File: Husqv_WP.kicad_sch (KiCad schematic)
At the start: 10 parts, among them U1 TC4421, U2 TC4422

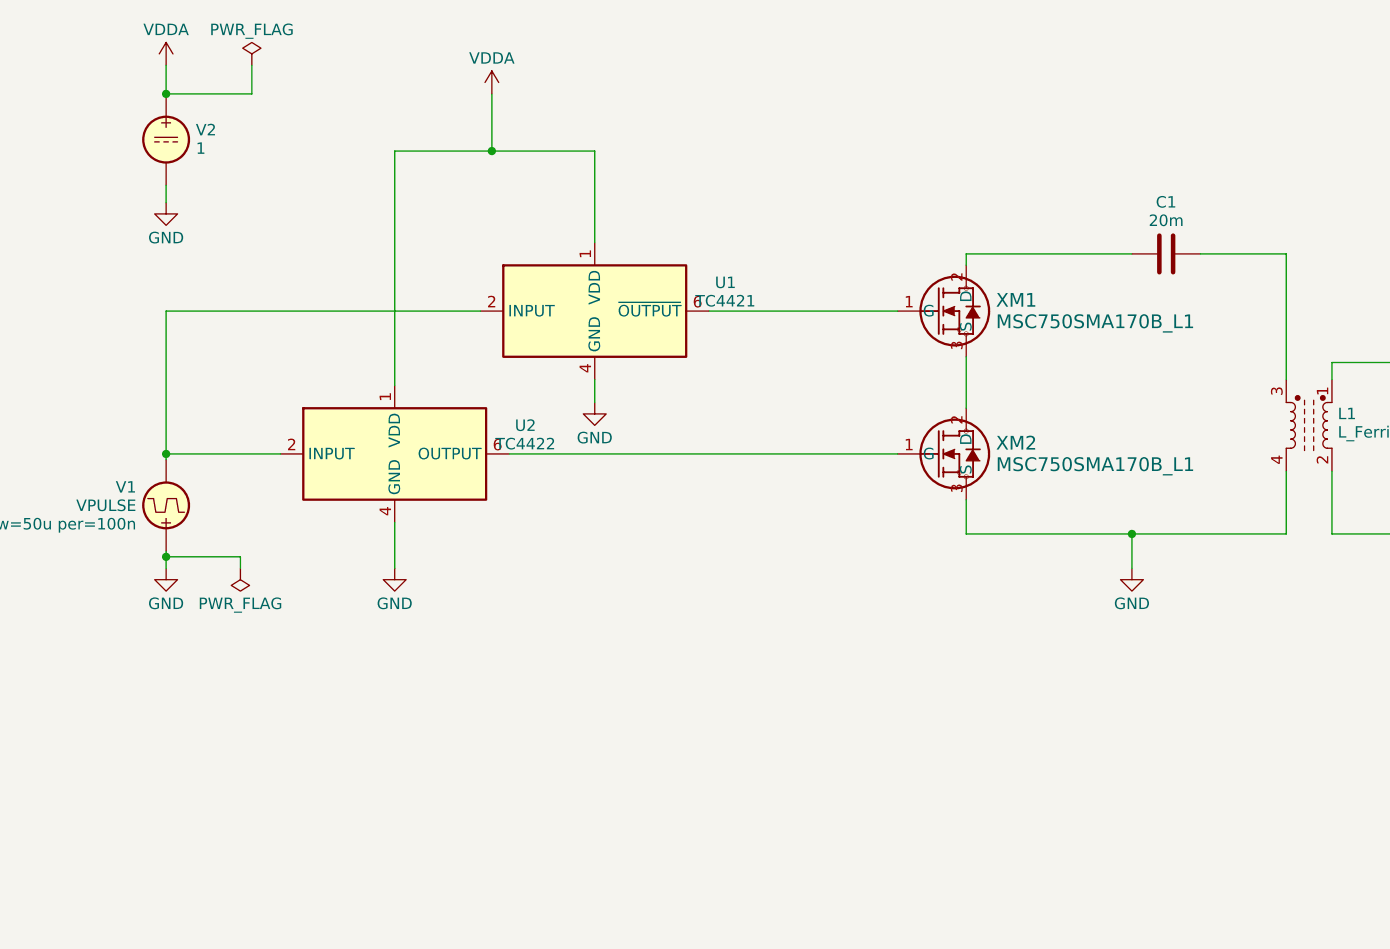
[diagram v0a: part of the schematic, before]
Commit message: working ... and changing branch names for new LLC topologies (so I can use only low-side FET drivers)
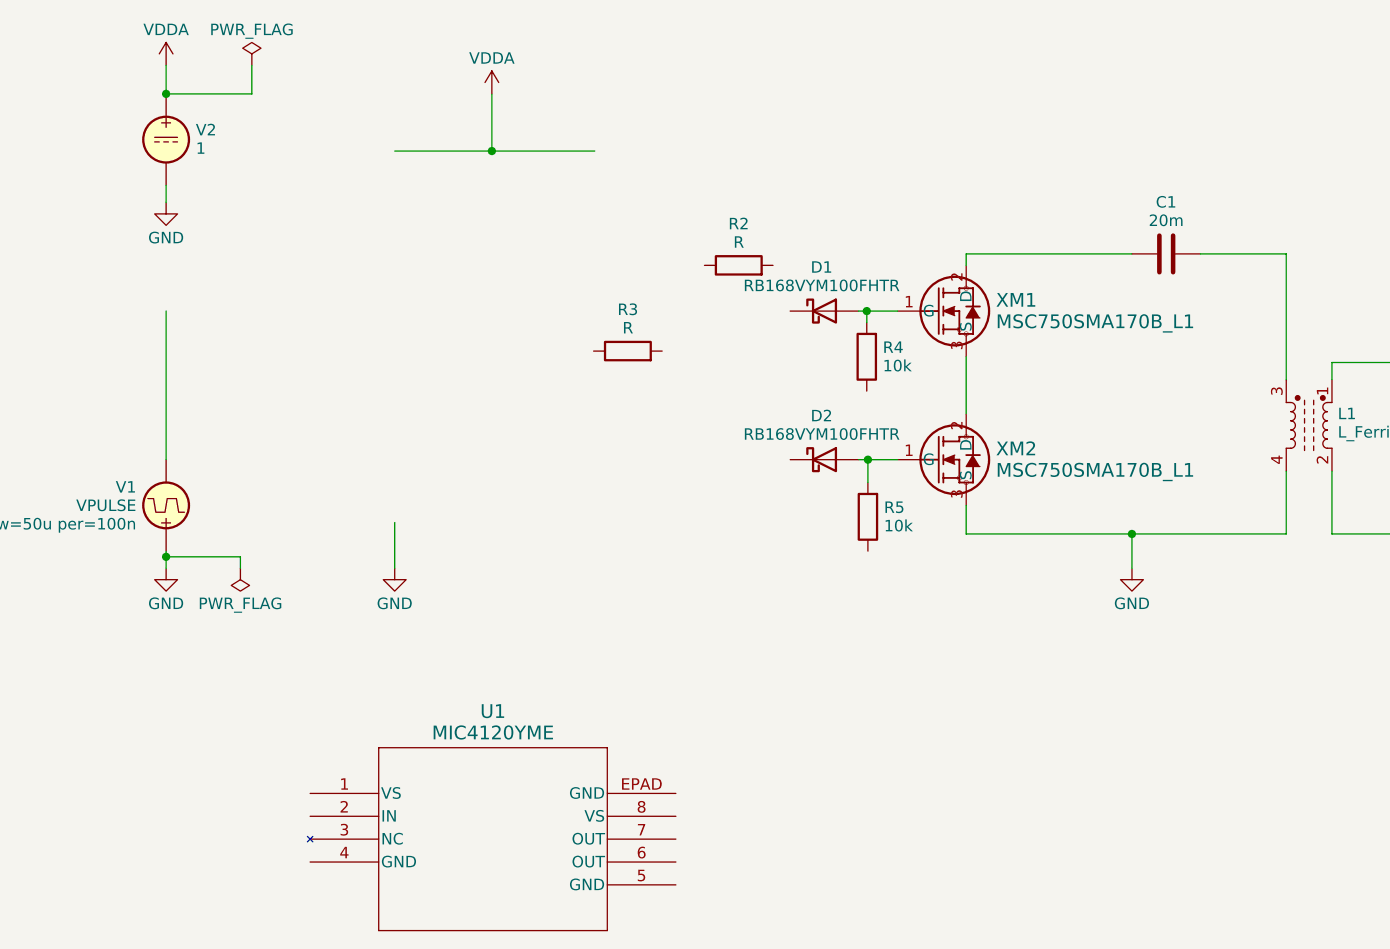
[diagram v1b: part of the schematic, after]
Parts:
- removed U1: TC4421, Package_DIP:DIP-8-N6_W7.62mm, symbol Driver_FET:TC4421
- removed U2: TC4422, Package_DIP:DIP-8-N6_W7.62mm, symbol Driver_FET:TC4422
- added D1, D2: RB168VYM100FHTR, Diode_SMD:D_SOD-323_HandSoldering, symbol Device:D_Schottky
- added R2, R3: R, symbol Device:R
- added R4, R5: 10k, Resistor_SMD:R_0603_1608Metric_Pad0.98x0.95mm_HandSolder, symbol Device:R
- added U1: MIC4120YME, SOIC8_EPAD_ME_MCH, symbol myLibSymbols:MIC4120YME
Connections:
- net at XM1.1 (G): now also D1.2 (A), R4.2
- net at XM2.1 (G): now also D2.2 (A), R5.2
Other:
- moved on the sheet: XM2

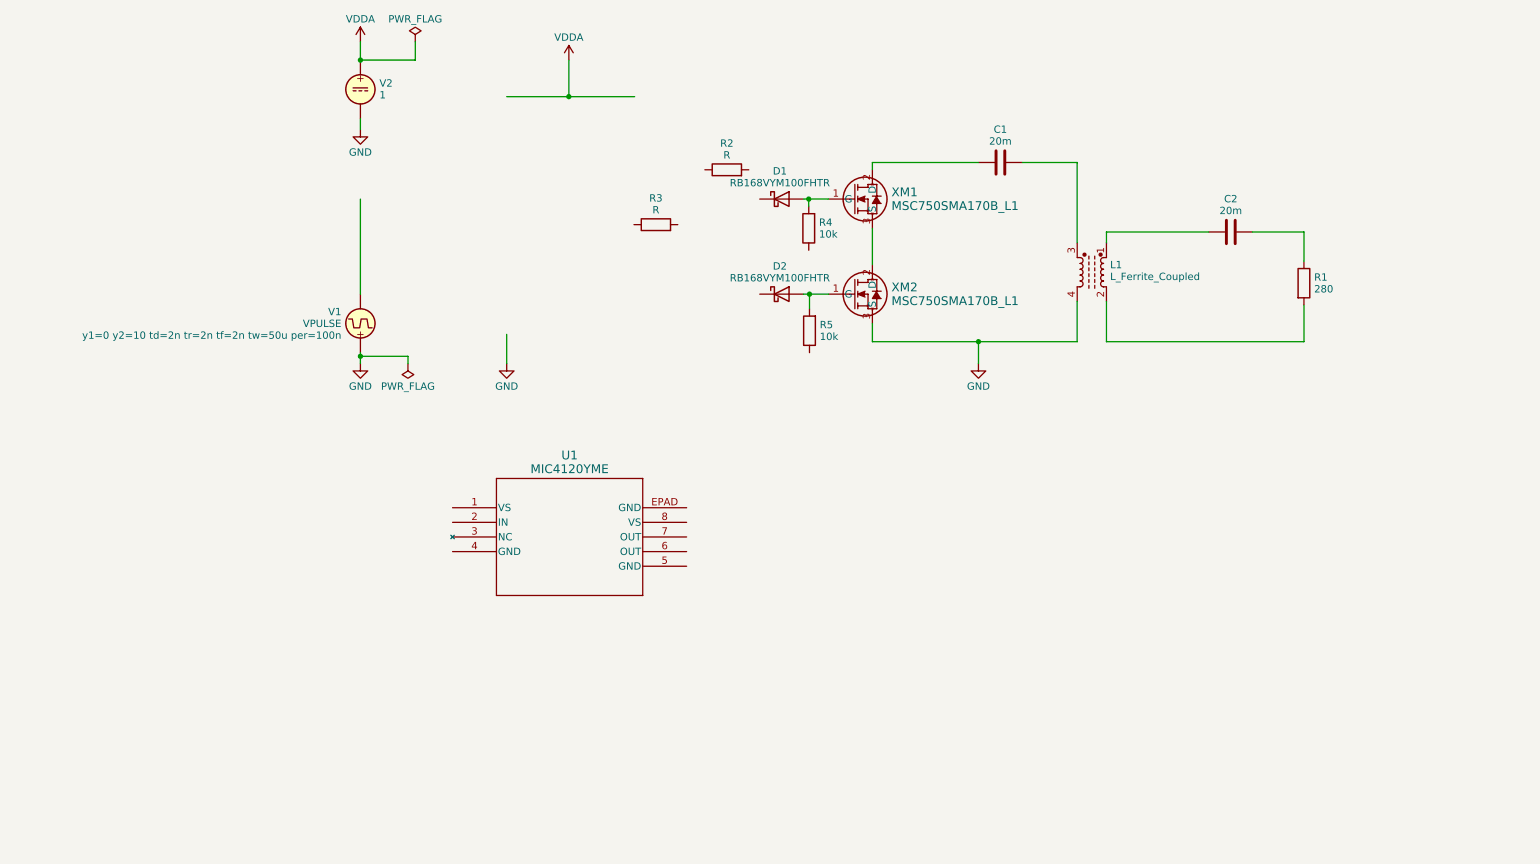
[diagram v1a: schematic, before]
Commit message: working: plot works and two Vpulse is used. Will nowvswap them for and AC source and try an AC sweep
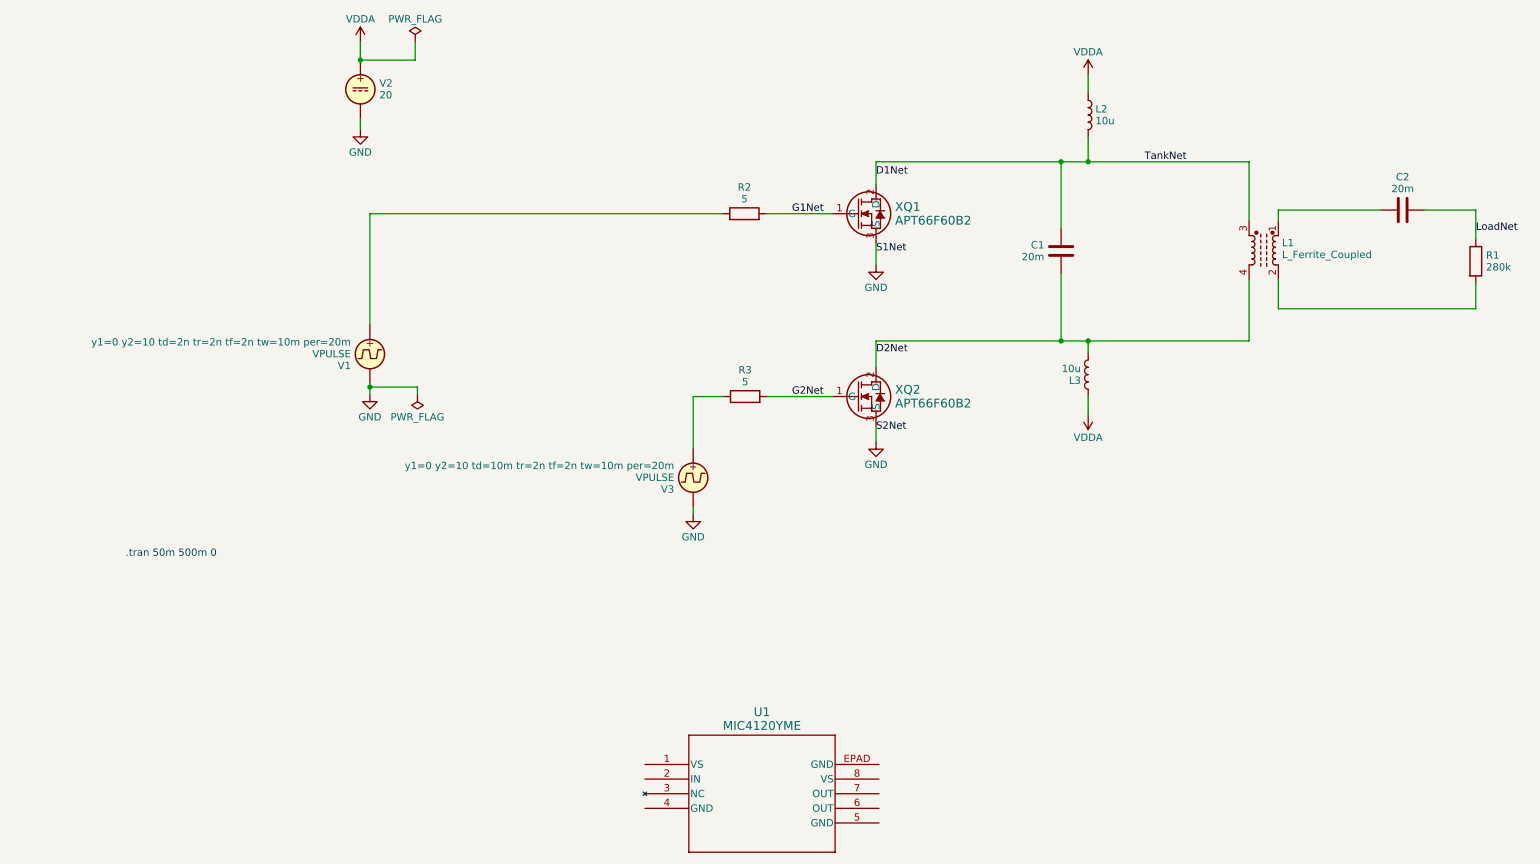
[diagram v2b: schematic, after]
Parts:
- removed D1, D2: RB168VYM100FHTR, Diode_SMD:D_SOD-323_HandSoldering, symbol Device:D_Schottky
- removed R4, R5: 10k, Resistor_SMD:R_0603_1608Metric_Pad0.98x0.95mm_HandSolder, symbol Device:R
- removed XM1: MSC750SMA170B_L1, TO-247_MCH, symbol myLibSymbols:MSC750SMA170B
- added L2, L3: 10u, symbol Device:L
- added V3: VPULSE, symbol Simulation_SPICE:VPULSE
- added XQ1: APT66F60B2, TO-247_MCH, symbol myLibSymbols:MSC750SMA170B
- R1: value 280 -> 280k
- R2, R3: value R -> 5
- V2: value 1 -> 20
- XQ2: renamed from XM2; value MSC750SMA170B_L1 -> APT66F60B2
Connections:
- net GND: now also V1.2, V3.2, XQ1.3 (S); no longer L1.4, V1.1
- net VDDA: now also L2.1, L3.1
- net G2Net: now reaches XQ2.1 (G)
- net G2Net: now also R3.2
- net D2Net: now reaches C1.1
- net D2Net: now also L1.4, XQ2.2 (D), L3.2
- net LoadNet: now reaches C2.2, R1.1
- net at R3.1: now also V3.1
- net at R2.1: now also V1.1
- net G1Net: now reaches R2.2
- net G1Net: now also XQ1.1 (G)
- net D1Net: now reaches C1.2, L1.3
- net D1Net: now also L2.2, XQ1.2 (D)
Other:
- note added: ".tran 50m 500m 0"
- moved on the sheet: C2, L1, R1, R2, R3, U1, XQ2
